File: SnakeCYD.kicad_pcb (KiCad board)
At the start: 2 copper layers, 37 parts, among them J1 USB_C_Receptacle_USB2.0_16P, J2 UART, J3 I2C_1, J4 SPI, J5 I2C_2, J6 0UART, J7 GPIO, SW1 SW_MEC_5E, SW2 SW_MEC_5E, SW3 SW_MEC_5E, U1 ESP32-S3-WROOM-1, U2 TFT_320x240, U3 AMS1117-3.3

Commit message: well placed all the compnents in their places (PCB)
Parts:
- Boot: renamed from SW1; footprint Button_Switch_SMD:SW_Push_1P1T_NO_CK_KMR2 -> RAM:SW_Push_1P1T_NO_CK_KMR2; moved to B.Cu
- C1, C10, C11, C2, C3, C4, C5, C6, C7, C8, C9, D1, D5, D6, D7, D8, D9, J1, J2, J3, J4, J5, J6, J7, R1, R2, R3, R4, R5, R6, R7, U1, U3: moved to B.Cu
- ON/OFF: renamed from SW3; footprint Button_Switch_SMD:SW_Push_1P1T_NO_CK_KMR2 -> RAM:SW_Push_1P1T_NO_CK_KMR2; moved to B.Cu
- RST: renamed from SW2; footprint Button_Switch_SMD:SW_Push_1P1T_NO_CK_KMR2 -> RAM:SW_Push_1P1T_NO_CK_KMR2; moved to B.Cu
- moved D1 95.2 mm to (118.5, 97.0), turned to 180 degrees
- moved D5 80.3 mm to (146.0, 126.0), turned to 90 degrees
- moved D9 74.9 mm to (148.3, 129.7), turned to 90 degrees
- moved U2 73.5 mm to (191.2, 112.9), turned to 90 degrees
- moved D8 73.4 mm to (150.7, 129.7), turned to 90 degrees
- moved D6 72.8 mm to (157.5, 133.0), turned to -90 degrees
- moved D7 72.1 mm to (153.0, 129.7), turned to 90 degrees
- moved J3 71.6 mm to (124.8, 135.7), turned to 180 degrees
- moved J7 68.7 mm to (115.8, 90.9), turned to -90 degrees
- moved J1 65.1 mm to (150.4, 137.3), turned to 180 degrees
- moved J2 63.9 mm to (108.8, 103.5), turned to 90 degrees
- moved J5 63.3 mm to (109.0, 130.0), turned to 90 degrees
- moved U3 58.7 mm to (163.5, 126.5), turned to 90 degrees
- moved C1 48.7 mm to (146.0, 129.5), turned to -90 degrees
- moved C8 42.6 mm to (187.0, 136.5), turned to 90 degrees
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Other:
- board outline added: 95 x 57 mm

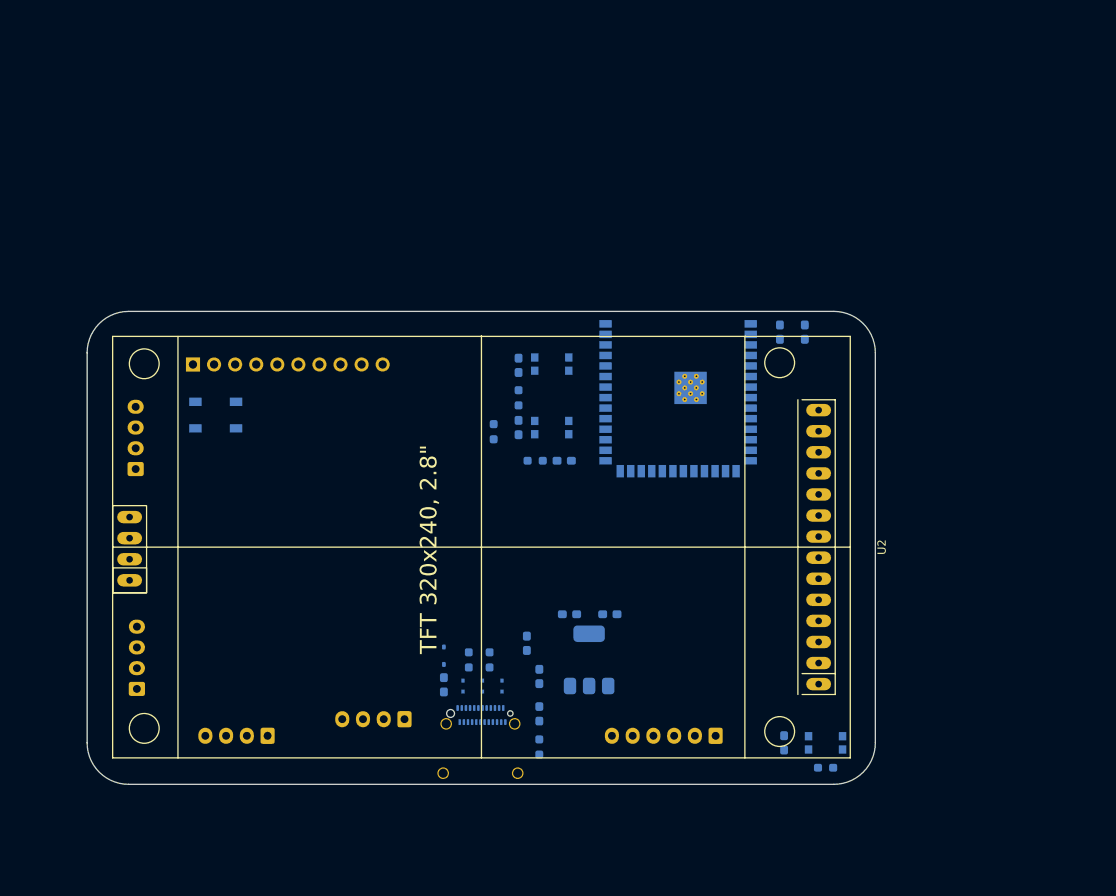
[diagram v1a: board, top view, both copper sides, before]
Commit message: Traced most of the components (PCB)
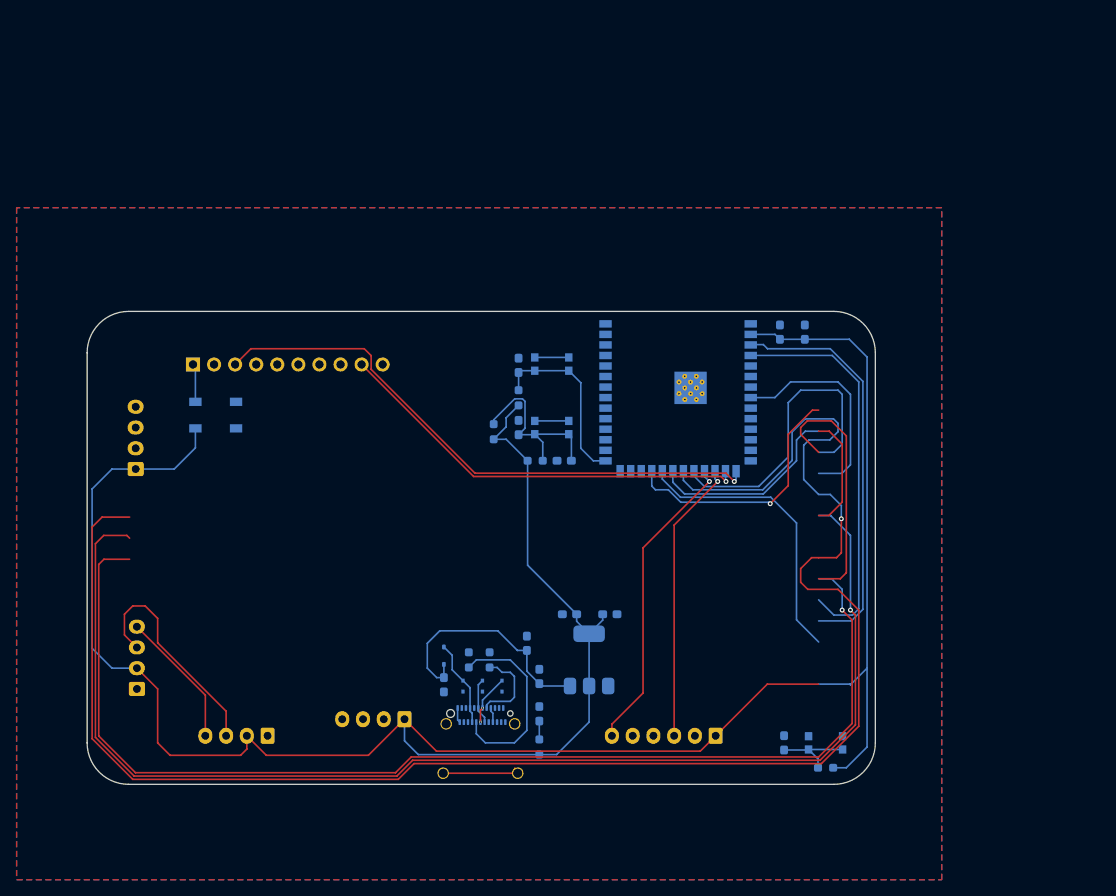
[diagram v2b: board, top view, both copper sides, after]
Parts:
- removed U2: TFT_320x240, Display-extra:TFT-320x240
- turned R3 to 90 degrees
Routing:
- net ESP_3v3: track 0.00 -> 291.6 mm
- net SPI2_MOSI: track 0.00 -> 207.4 mm, vias 0 -> 1
- net SPI2_CLK: track 0.00 -> 204.8 mm, vias 0 -> 1
- net SPI2_MISO: track 0.00 -> 190.1 mm, vias 0 -> 1
- net TFT_RST: track 0.00 -> 71.6 mm
- net ADC1_IO3: track 0.00 -> 69.9 mm, vias 0 -> 1
- net GPIO46: track 0.00 -> 51.0 mm, vias 0 -> 1
- net TFT_DC: track 0.00 -> 47.6 mm
- net ANY_CS: track 0.00 -> 37.0 mm, vias 0 -> 1
- net TFT_CS: track 0.00 -> 34.8 mm
- net SPI_MISO: track 0.00 -> 34.2 mm, vias 0 -> 1
- net T_IRQ: track 0.00 -> 31.1 mm, vias 0 -> 1
- net VCC_5v: track 0.00 -> 29.1 mm
- net SDA: track 0.00 -> 27.2 mm
- net T_CS: track 0.00 -> 26.2 mm
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- added copper zone on B.Cu, net GND
- added copper zone on F.Cu, net GND

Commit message: Finished tracing and fixing all the PCB
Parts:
- added U2: TFT_320x240, Display-extra:TFT-320x240, F.Cu at (191.2, 112.9)
- renumbered Boot to SW1, RST to SW2, ON/OFF to SW3
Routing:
- net SD_CS: track 0.00 -> 170.5 mm, vias 0 -> 3
- net SDA: track 27.2 -> 144.5 mm, vias 0 -> 5
- net SCL: track 16.6 -> 126.2 mm, vias 0 -> 5
- net Dp: track 5.52 -> 114.1 mm
- net RX: track 0.00 -> 106.7 mm, vias 0 -> 1
- net TX: track 0.00 -> 103.1 mm, vias 0 -> 1
- net Add_but: track 9.75 -> 106.9 mm, vias 0 -> 2
- net 0TX: track 0.00 -> 82.7 mm, vias 0 -> 3
- net 0RX: track 0.00 -> 81.2 mm, vias 0 -> 3
- net Dn: track 6.07 -> 73.6 mm, vias 2 -> 3
- net GPIO39: track 0.00 -> 59.7 mm, vias 0 -> 1
- net GPIO40: track 0.00 -> 59.1 mm, vias 0 -> 1
- net GPIO41: track 0.00 -> 58.4 mm, vias 0 -> 1
- net GPIO42: track 0.00 -> 57.9 mm, vias 0 -> 1
- net SPI_MOSI: track 0.00 -> 57.1 mm, vias 0 -> 7
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
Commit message: Slikscreen labeled all the pins
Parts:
- added G***: LOGO, LOGO, B.Cu at (118.1, 106.4)
- added G***: LOGO, LOGO, B.Cu at (130.5, 110.5)
- renumbered SW1 to Boot, SW3 to On/Off, SW2 to RST
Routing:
- net GND: vias 20 -> 27
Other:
- board text added: "CS"
- board text added: "GND"
- board text added: "I2C"
- board text added: "I2C_2"
- board text added: "IO2~"
- board text added: "IO39"
- board text added: "IO3~"
- board text added: "IO40"
- board text added: "IO41"
- board text added: "IO42"
- board text added: "IO45"
- board text added: "IO46"
- board text added: "IO48"
- board text added: "MISO"
- board text added: "MOSI"
- board text added: "Made with love by Nadoooor"
- board text added: "RGB"
- board text added: "SCK"
- board text added: "SCL"
- board text added: "SDA"
- board text added: "SPI"
- board text added: "UART"
- board text added: "USB>UART"
- board text added: "VCC"
